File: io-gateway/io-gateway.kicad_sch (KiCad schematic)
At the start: 14 parts, among them J1 1752201, J10 Screw_Terminal_01x02, J11 Screw_Terminal_01x02, J12 Screw_Terminal_01x02, J13 Screw_Terminal_01x02, J2 1752201, J3 1752201, J4 Screw_Terminal_01x02, J5 Screw_Terminal_01x02, J7 Screw_Terminal_01x02, J8 Screw_Terminal_01x02, J9 Screw_Terminal_01x02

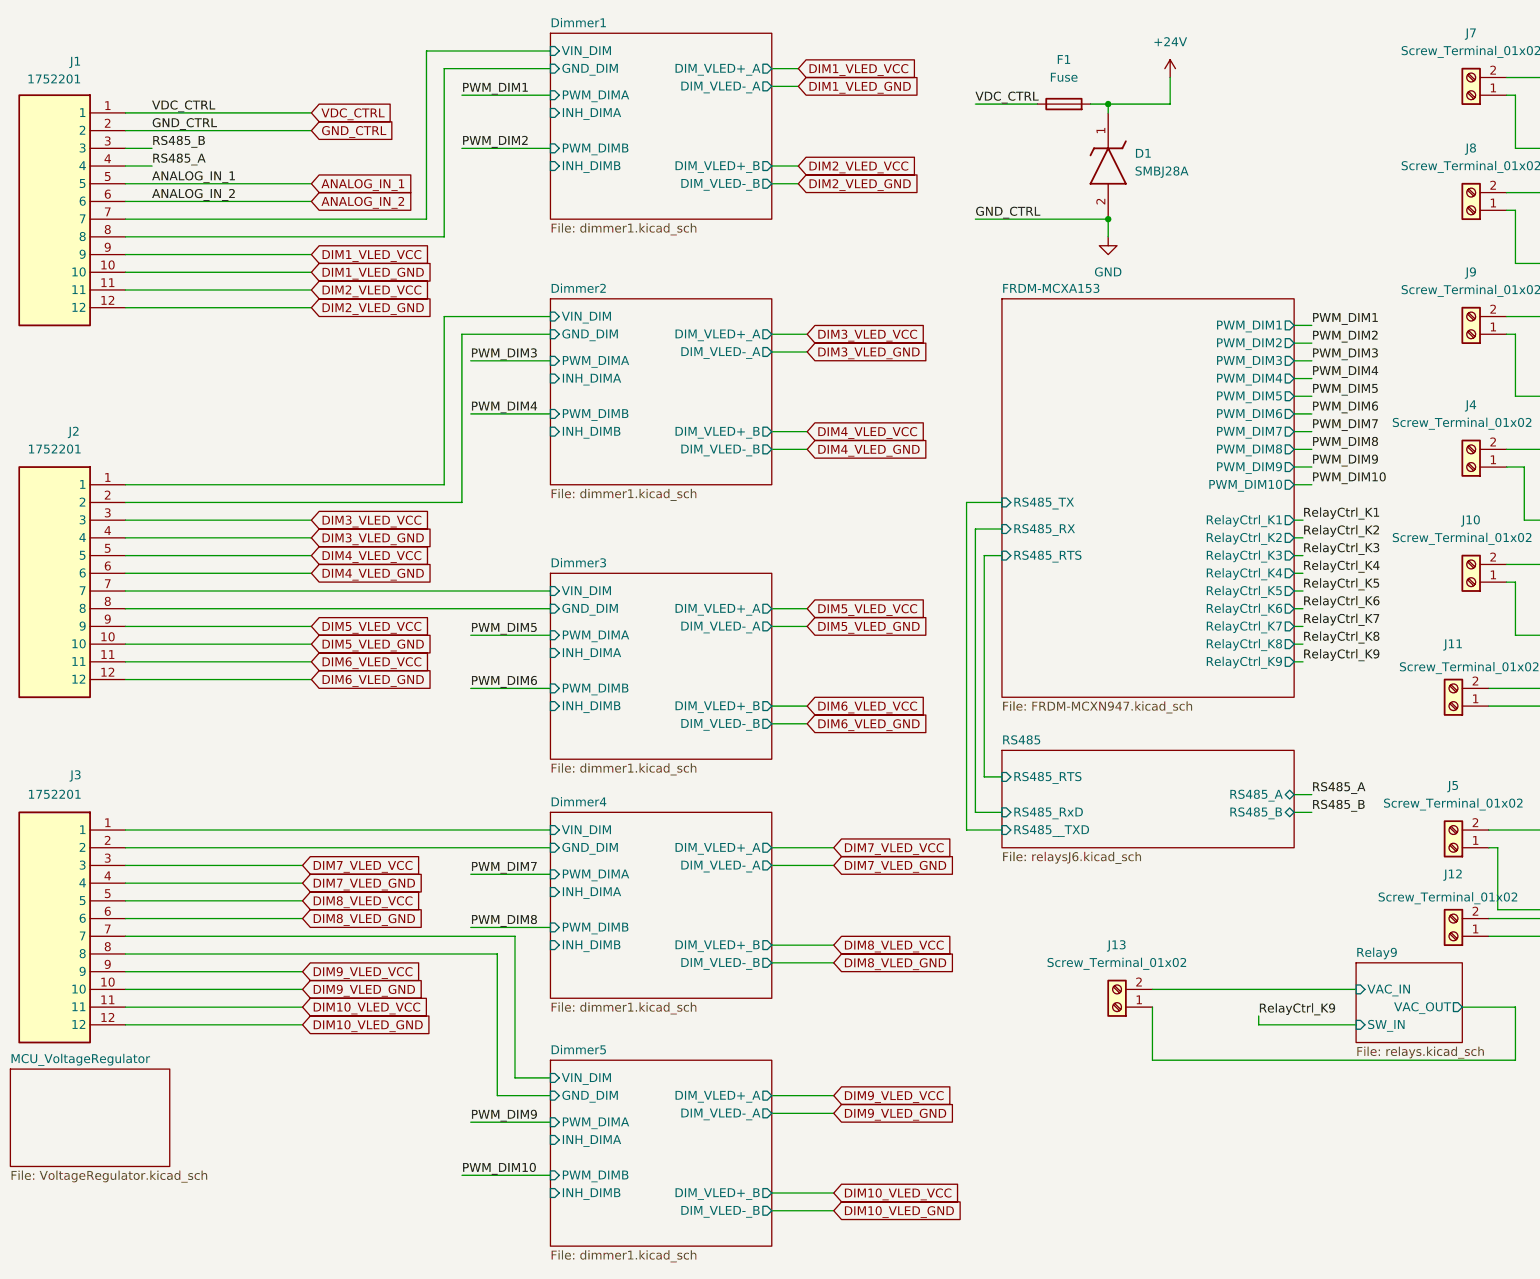
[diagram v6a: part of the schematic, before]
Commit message: connect inh pins
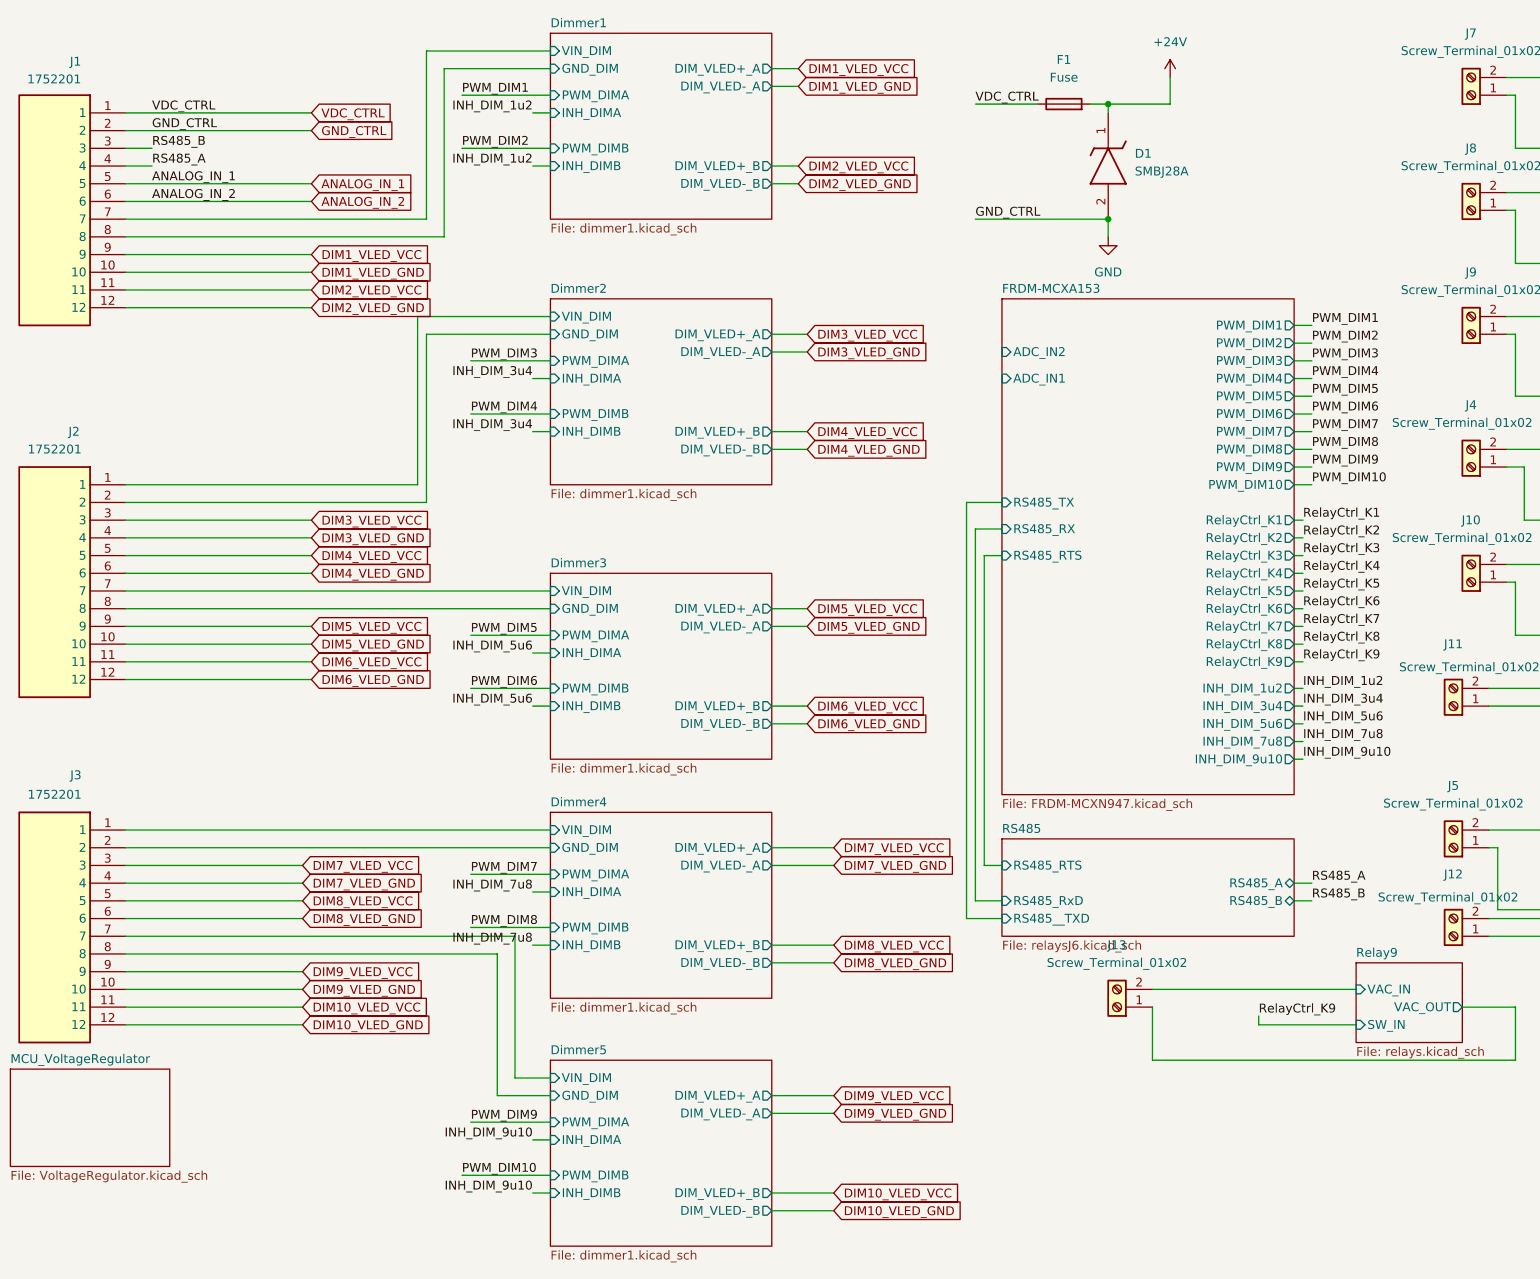
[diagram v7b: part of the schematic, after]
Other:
- sheet FRDM-MCXA153 ports: added ADC_IN1, ADC_IN2, INH_DIM_1u2, INH_DIM_3u4, INH_DIM_5u6, INH_DIM_7u8, INH_DIM_9u10; removed none

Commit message: upd
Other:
- sheet RS485 ports: added RS485_TXD; removed RS485__TXD
